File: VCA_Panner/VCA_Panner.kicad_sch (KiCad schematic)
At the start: 81 parts, among them J1 CV1, J2 CV2, J3 Ch1_in, J4 Ch2_in, J5 Ch1_out, J6 Ch2_out, U1 AS3360, U2 TL074, U3 TL074, U4 TL074, U5 LM358

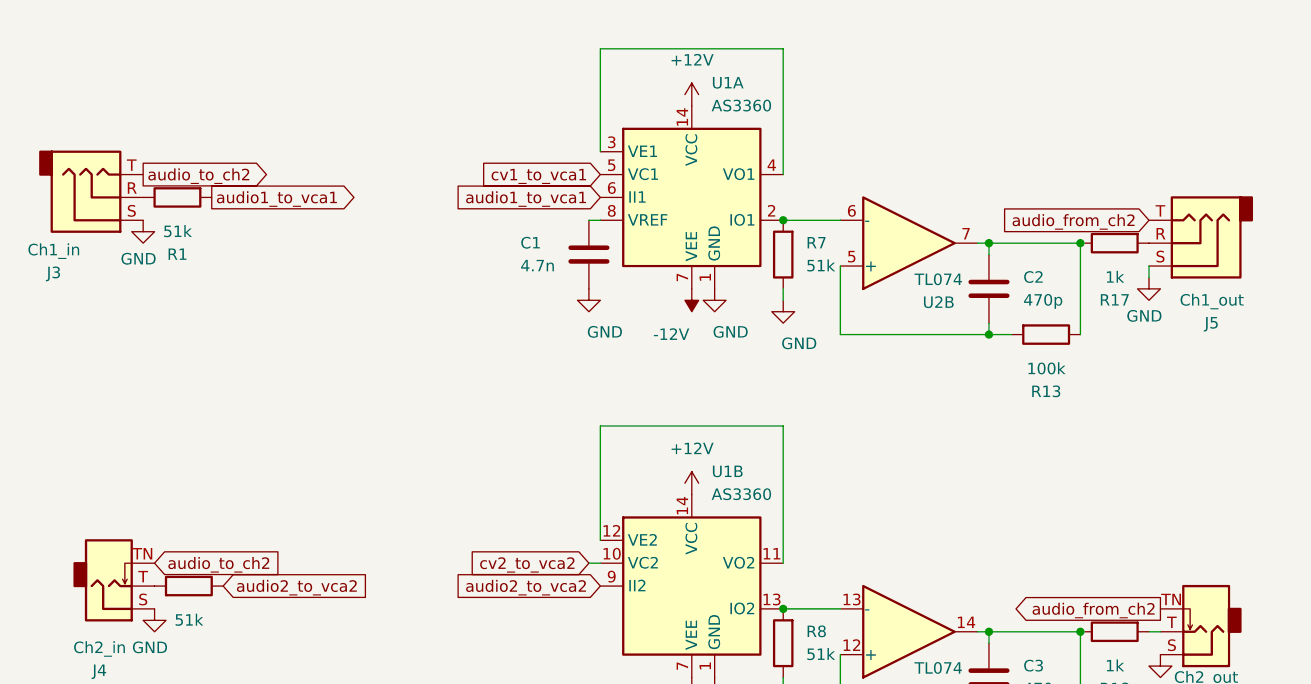
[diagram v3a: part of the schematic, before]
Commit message: vca panner
All done, first set ordered
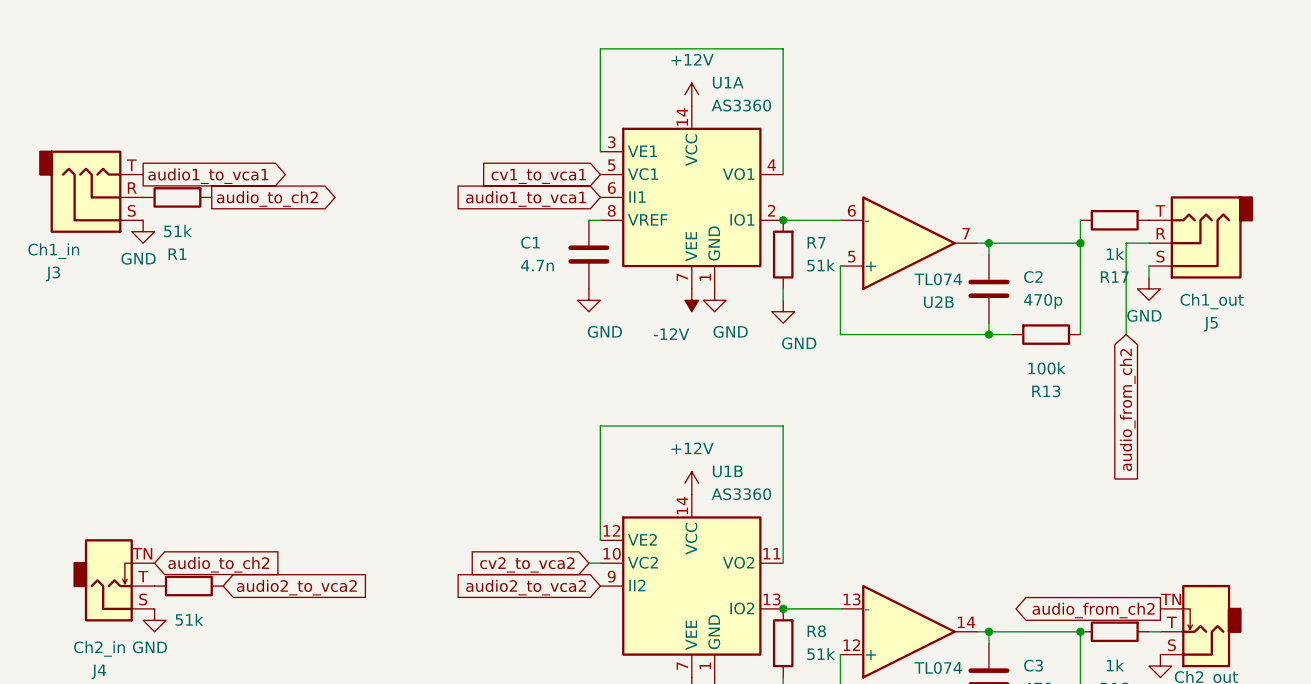
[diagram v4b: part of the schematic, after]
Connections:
- net audio1_to_vca1: now also J3.T; no longer R1.2
- net audio_from_ch2: now also J5.R; no longer J5.T
- net audio_to_ch2: now also R1.2; no longer J3.T
- net at R17.2: now also J5.T; no longer J5.R
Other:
- moved on the sheet: R17
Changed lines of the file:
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@@
 	(wire
 		(pts
+			(xy 137.16 137.16) (xy 139.7 137.16)
+		)
+		(stroke
+			(width 0)
+			(type default)
+		)
+	)
+	(wire
+		(pts
 			(xy 99.06 177.8) (xy 105.41 177.8)
 		)
@@
 	(wire
 		(pts
+			(xy 132.08 134.62) (xy 132.08 137.16)
+		)
+		(stroke
+			(width 0)
+			(type default)
+		)
+	)
+	(wire
+		(pts
 			(xy 173.99 29.21) (xy 170.18 29.21)
 		)
@@
 	(wire
 		(pts
+			(xy 137.16 147.32) (xy 137.16 137.16)
+		)
+		(stroke
+			(width 0)
+			(type default)
+		)
+	)
+	(wire
+		(pts
 			(xy 125.73 73.66) (xy 125.73 77.47)
 		)
@@
 		)
 	)
+	(global_label "audio_to_ch2"
+		(shape output)
+		(at 35.56 132.08 0)
+		(fields_autoplaced yes)
+		(effects
+			(font
+				(size 1.27 1.27)
+			)
+			(justify left)
+		)
+		(property "Intersheetrefs" "${INTERSHEET_REFS}"
+			(at 51.003 132.08 0)
+			(effects
+				(font
+					(size 1.27 1.27)
+				)
+				(justify left)
+				(hide yes)
+			)
+		)
+	)
 	(global_label "CV2"
 		(shape input)
@@
 		)
 	)
-	(global_label "audio_from_ch2"
-		(shape input)
-		(at 139.7 134.62 180)
-		(fields_autoplaced yes)
-		(effects
-			(font
-				(size 1.27 1.27)
-			)
-			(justify right)
-		)
-		(property "Intersheetrefs" "${INTERSHEET_REFS}"
-			(at 121.7775 134.62 0)
-			(effects
-				(font
-					(size 1.27 1.27)
-				)
-				(justify right)
-				(hide yes)
-			)
-		)
-	)
 	(global_label "cv2_to_vca2"
 		(shape output)
@@
 		)
 	)
-	(global_label "audio1_to_vca1"
+	(global_label "audio_from_ch2"
 		(shape output)
-		(at 35.56 132.08 0)
+		(at 140.97 177.8 180)
 		(fields_autoplaced yes)
 		(effects
@@
 				(size 1.27 1.27)
 			)
-			(justify left)
+			(justify right)
 		)
 		(property "Intersheetrefs" "${INTERSHEET_REFS}"
-			(at 51.9706 132.08 0)
+			(at 123.0475 177.8 0)
 			(effects
 				(font
 					(size 1.27 1.27)
 				)
-				(justify left)
+				(justify right)
 				(hide yes)
 			)
 		)
 	)
-	(global_label "audio_from_ch2"
-		(shape output)
-		(at 140.97 177.8 180)
+	(global_label "audio1_to_vca1"
+		(shape input)
+		(at 78.74 132.08 180)
 		(fields_autoplaced yes)
 		(effects
@@
 		)
 		(property "Intersheetrefs" "${INTERSHEET_REFS}"
-			(at 123.0475 177.8 0)
+			(at 61.1199 132.08 0)
 			(effects
 				(font
@@
 		)
 	)
-	(global_label "audio1_to_vca1"
-		(shape input)
-		(at 78.74 132.08 180)
+	(global_label "CV2"
+		(shape output)
+		(at 35.56 72.39 0)
 		(fields_autoplaced yes)
 		(effects
@@
 				(size 1.27 1.27)
 			)
-			(justify right)
+			(justify left)
 		)
 		(property "Intersheetrefs" "${INTERSHEET_REFS}"
-			(at 61.1199 132.08 0)
+			(at 42.1133 72.39 0)
 			(effects
 				(font
 					(size 1.27 1.27)
 				)
-				(justify right)
+				(justify left)
 				(hide yes)
 			)
 		)
 	)
-	(global_label "audio_to_ch2"
+	(global_label "audio1_to_vca1"
 		(shape output)
 		(at 27.94 129.54 0)
@@
 		)
 		(property "Intersheetrefs" "${INTERSHEET_REFS}"
-			(at 43.383 129.54 0)
+			(at 44.3506 129.54 0)
 			(effects
 				(font
@@
 		)
 	)
-	(global_label "CV2"
-		(shape output)
-		(at 35.56 72.39 0)
+	(global_label "audio_from_ch2"
+		(shape input)
+		(at 137.16 147.32 270)
 		(fields_autoplaced yes)
 		(effects
@@
 				(size 1.27 1.27)
 			)
-			(justify left)
+			(justify right)
 		)
 		(property "Intersheetrefs" "${INTERSHEET_REFS}"
-			(at 42.1133 72.39 0)
+			(at 137.16 165.2425 90)
 			(effects
 				(font
 					(size 1.27 1.27)
 				)
-				(justify left)
+				(justify right)
 				(hide yes)
 			)
@@
 	(symbol
 		(lib_id "Device:R")
-		(at 135.89 137.16 90)
+		(at 135.89 134.62 90)
 		(mirror x)
 		(unit 1)
@@
 		(dnp no)
 		(property "Reference" "R17"
-			(at 135.89 143.51 90)
+			(at 135.89 140.97 90)
 			(effects
 				(font
@@
 		)
 		(property "Value" "1k"
-			(at 135.89 140.97 90)
+			(at 135.89 138.43 90)
 			(effects
 				(font
@@
 		)
 		(property "Footprint" "Resistor_SMD:R_0805_2012Metric_Pad1.20x1.40mm_HandSolder"
-			(at 135.89 135.382 90)
+			(at 135.89 132.842 90)
 			(effects
 				(font
@@
 		)
 		(property "Datasheet" "~"
-			(at 135.89 137.16 0)
+			(at 135.89 134.62 0)
 			(effects
 				(font
@@
 		)
 		(property "Description" "Resistor"
-			(at 135.89 137.16 0)
+			(at 135.89 134.62 0)
 			(effects
 				(font

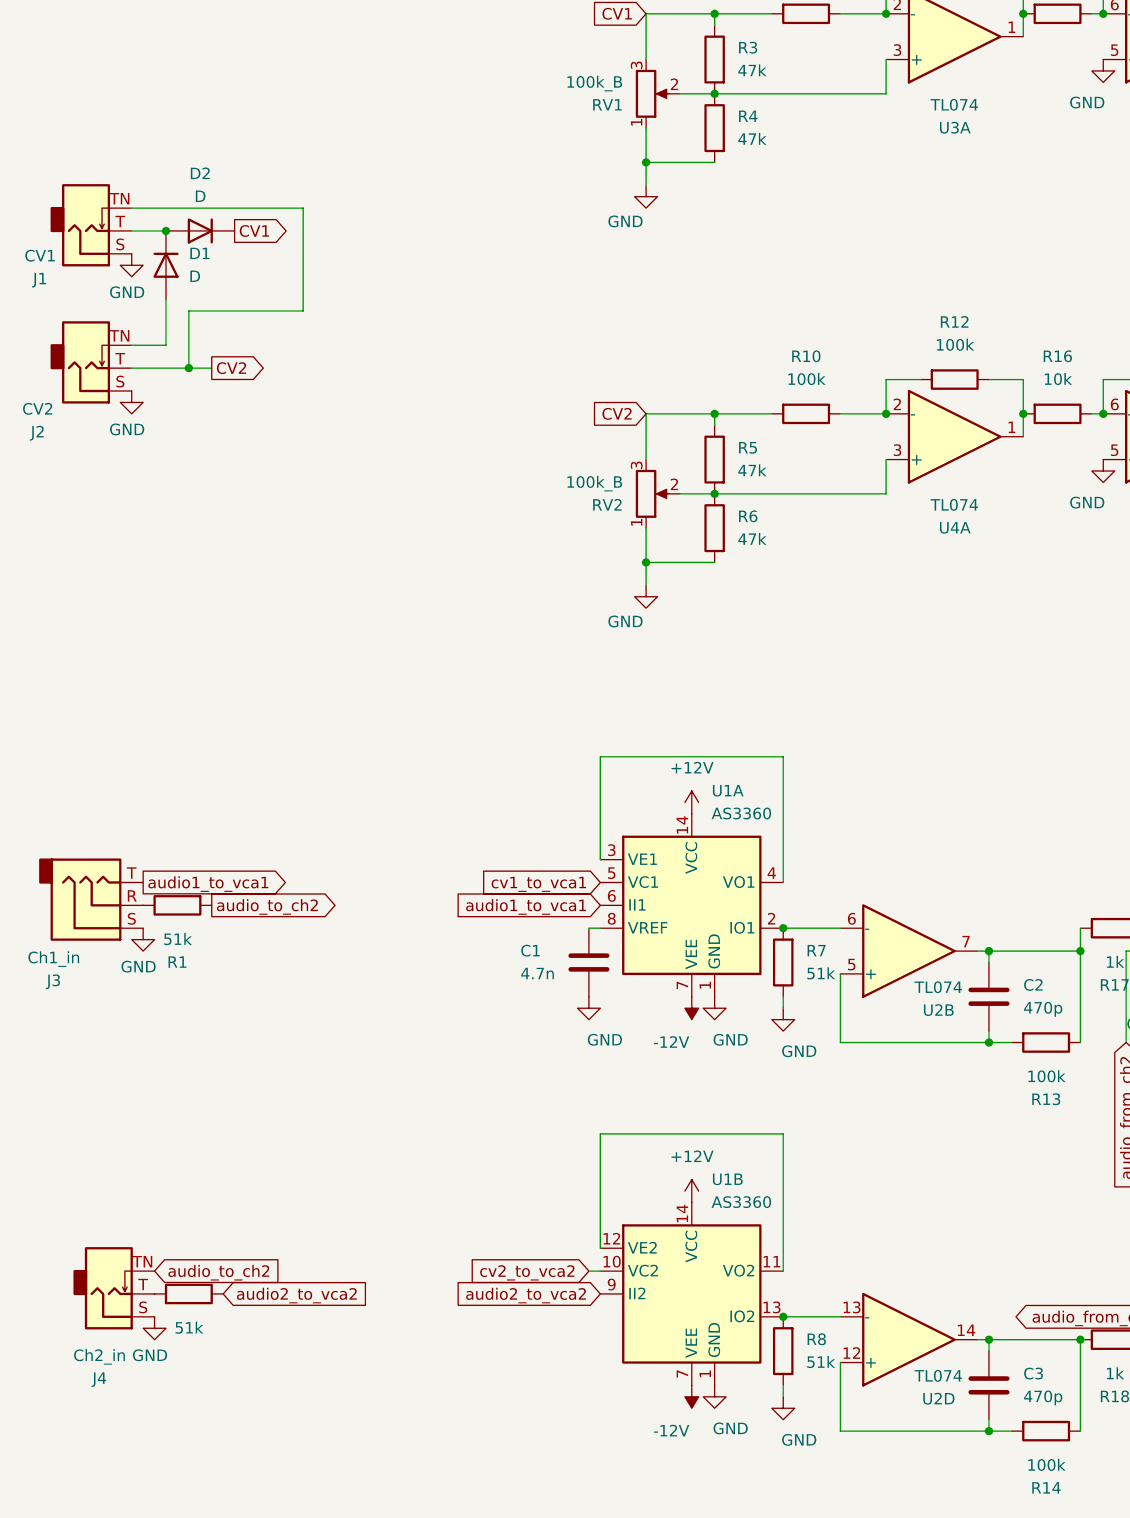
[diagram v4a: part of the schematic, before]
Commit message: vca panner fixes
fixed the footprint and audio routing. ditched the diodes for cv splitting.
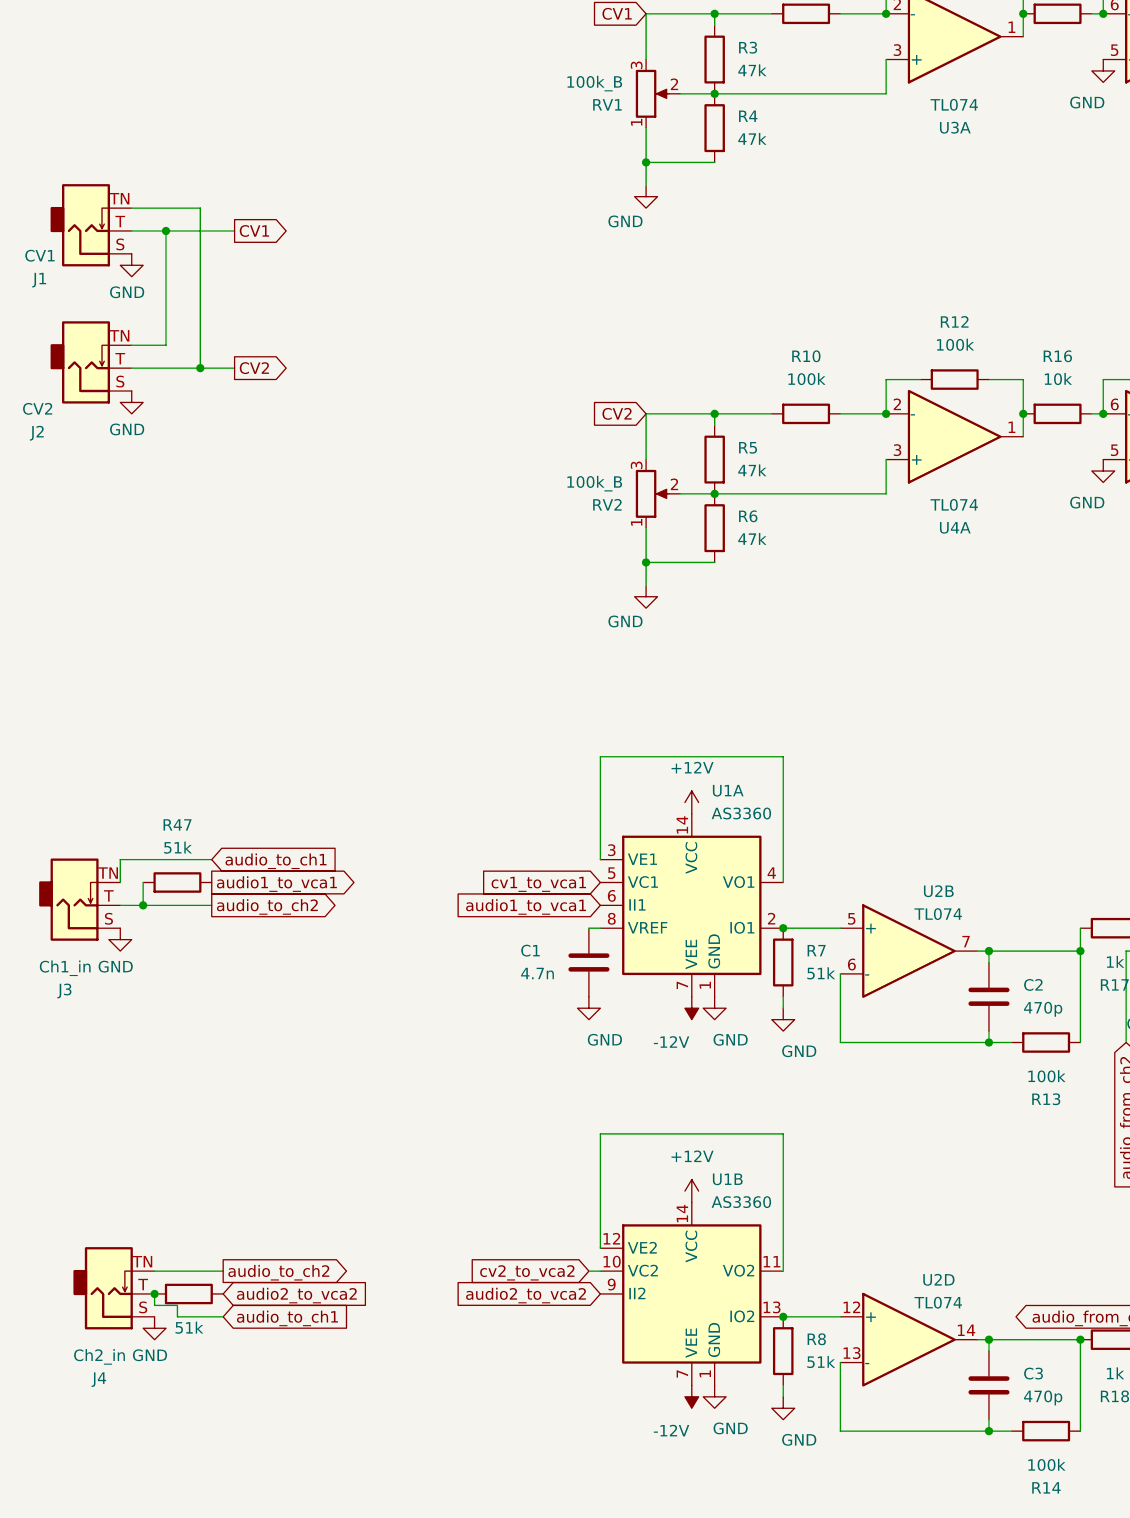
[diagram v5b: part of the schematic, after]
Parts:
- removed D1, D2: D, Diode_SMD:D_0805_2012Metric_Pad1.15x1.40mm_HandSolder, symbol Device:D
- removed J3: Ch1_in, mort_mix:Jack_3.5mm_QingPu_WQP-PJ366ST_Vertical, symbol Connector_Audio:AudioJack3
- removed R1: 51k, Resistor_SMD:R_0805_2012Metric_Pad1.20x1.40mm_HandSolder, symbol Device:R
- added J3: Ch1_in, mort_mix:PJ398SM, symbol Connector_Audio:AudioJack2_SwitchT
- added R47: 51k, Resistor_SMD:R_0805_2012Metric_Pad1.20x1.40mm_HandSolder, symbol Device:R
- U1: footprint Package_SO:SOIC-16_3.9x9.9mm_P1.27mm -> Package_SO:SO-14_3.9x8.65mm_P1.27mm
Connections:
- net CV1: now also J1.T, J2.TN
- net GND: now also J3.S
- net audio1_to_vca1: now also R47.1
- net audio_to_ch2: now also J3.T, R47.2
- net at C3.1, R14.2: now also U2.13 (-); no longer U2.12 (+)
- net at C2.1, R13.2: now also U2.6 (-); no longer U2.5 (+)
- net at R7.2, U1.2 (IO1): now also U2.5 (+); no longer U2.6 (-)
- net at R8.2, U1.13 (IO2): now also U2.12 (+); no longer U2.13 (-)
- net audio_to_ch1: now reaches J4.T, R2.2
- net audio_to_ch1: now also J3.TN
